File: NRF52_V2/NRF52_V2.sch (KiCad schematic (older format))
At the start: 0 parts

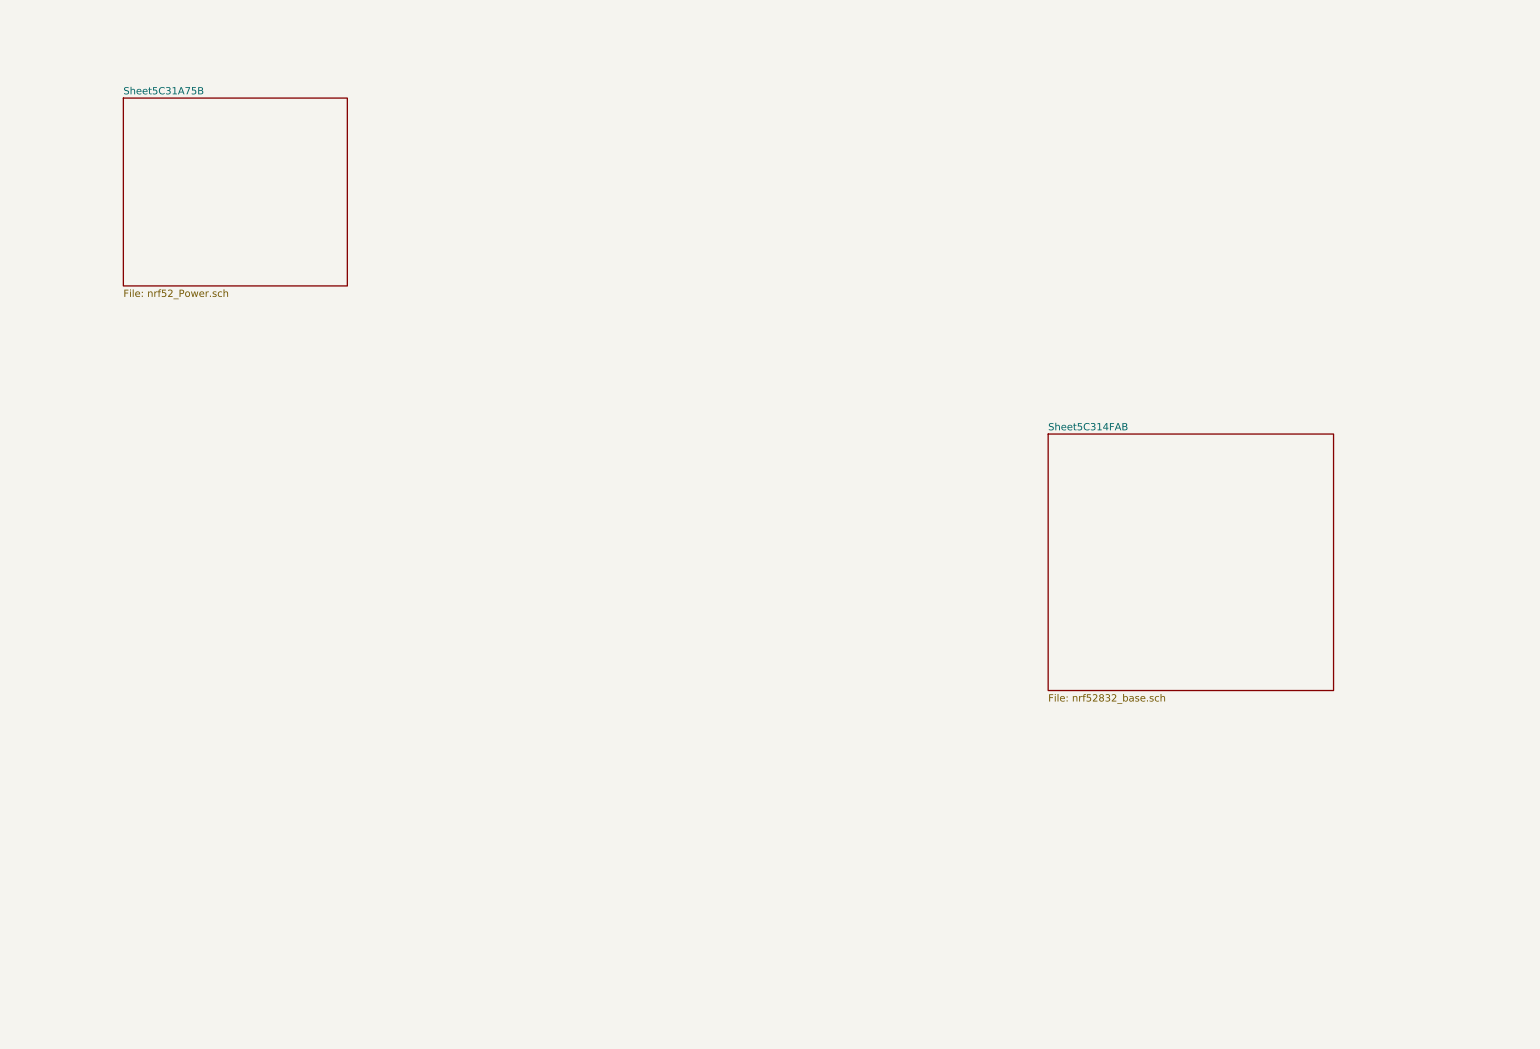
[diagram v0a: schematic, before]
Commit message: Added SWD header and some buttons
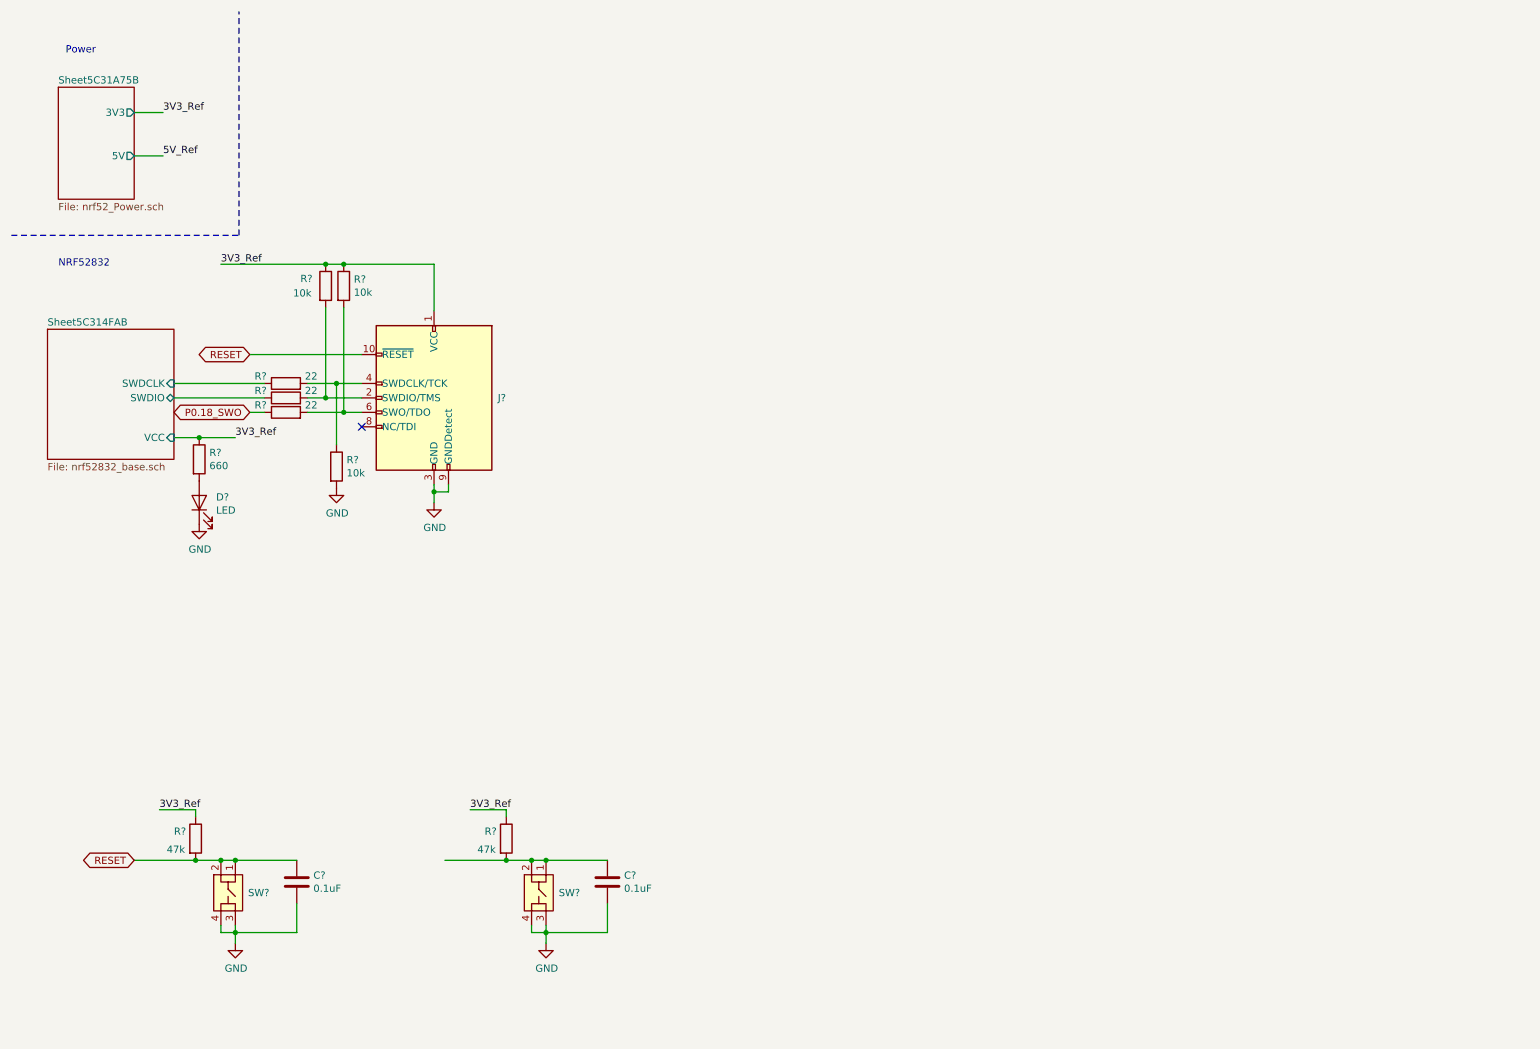
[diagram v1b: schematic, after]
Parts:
- added C? (x2): 0.1uF, symbol Device:C
- added D?: LED, symbol Device:LED
- added J?: Conn_ARM_JTAG_SWD_10, Connector_PinHeader_1.27mm:PinHeader_2x05_P1.27mm_Vertical_SMD, symbol Connector:Conn_ARM_JTAG_SWD_10
- added R? (x2): 47k, symbol Device:R
- added R?: 660, symbol Device:R
- added R? (x3): 22, symbol Device:R
- added R? (x3): 10k, symbol Device:R
- added SW? (x2): SW_SPST_4pin, symbol Project_Libary:SW_SPST_4pin
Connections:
- new net: C?.1, R?.2, SW?.1, SW?.2
- new net: D?.2 (A), R?.2
- new net: J?.2 (SWDIO/TMS), R?.2, R?.2
- new net: J?.4 (SWDCLK/TCK), R?.1, R?.2
- new net: J?.6 (SWO/TDO), R?.2, R?.2
- new net 3V3_Ref: J?.1 (VCC), R?.1, R?.1, R?.1, R?.1, R?.1
- new net GND: C?.2, C?.2, D?.1 (K), J?.3 (GND), J?.5 (GND), J?.9 (GNDDetect), R?.2, SW?.3, SW?.3, SW?.4, SW?.4
- new net P0.18_SWO: R?.1
- new net RESET: C?.1, J?.10 (~RESET~), R?.2, SW?.1, SW?.2
- new net Sheet5C314FAB/SWDCLK: R?.1
- new net Sheet5C314FAB/SWDIO: R?.1
- no-connect marks 0 -> 1
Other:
- note added: "NRF52832"
- note added: "Power"

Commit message: Added GPIO pin headers, buttons, and LEDs.
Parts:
- added D? (x2): LED, symbol Device:LED
- added J?: Conn_01x04_Male, symbol Connector:Conn_01x04_Male
- added J? (x2): Conn_01x05_Male, symbol Connector:Conn_01x05_Male
- added J? (x2): Conn_01x10_Male, symbol Connector:Conn_01x10_Male
- added R? (x2): 660, symbol Device:R
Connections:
- net 3V3_Ref: now also J?.9 (Pin_9); no longer J?.1 (VCC), R?.1, R?.1
- net 5V_Ref: now also J?.1 (VCC), R?.1, R?.1, J?.10 (Pin_10)
- net GND: now also D?.1 (K), D?.1 (K), J?.4 (Pin_4), J?.5 (Pin_5)
- net P0.18_SWO: now also J?.8 (Pin_8)
- net P0.24: now reaches C?.1, R?.2, SW?.1, SW?.2
- net P0.24: now also J?.3 (Pin_3)
- new net: D?.2 (A), R?.2 (x2)
- new net P0.02: J?.1 (Pin_1)
- new net P0.03: J?.2 (Pin_2)
- new net P0.04: J?.3 (Pin_3), R?.1
- new net P0.05: J?.4 (Pin_4), R?.1
- new net P0.06: J?.1 (Pin_1)
- new net P0.07: J?.2 (Pin_2)
- new net P0.08: J?.3 (Pin_3)
- new net P0.09: J?.4 (Pin_4)
- new net P0.10: J?.5 (Pin_5)
- new net P0.11_SDA: J?.1 (Pin_1)
- new net P0.12_SCL: J?.2 (Pin_2)
- new net P0.13: J?.3 (Pin_3)
- new net P0.14: J?.4 (Pin_4)
- new net P0.15: J?.5 (Pin_5)
- new net P0.16: J?.6 (Pin_6)
- new net P0.17: J?.7 (Pin_7)
- new net P0.19: J?.9 (Pin_9)
- new net P0.20: J?.10 (Pin_10)
- new net P0.22: J?.1 (Pin_1)
- new net P0.23: J?.2 (Pin_2)
- new net P0.25: J?.2 (Pin_2)
- new net P0.26: J?.3 (Pin_3)
- new net P0.27: J?.4 (Pin_4)
- new net P0.28: J?.5 (Pin_5)
- new net P0.29: J?.6 (Pin_6)
- new net P0.30: J?.7 (Pin_7)
- new net P0.31: J?.8 (Pin_8)
- new net V+: J?.1 (Pin_1)
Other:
- note added: "User I/O"
- moved on the sheet: C?, R?, SW?

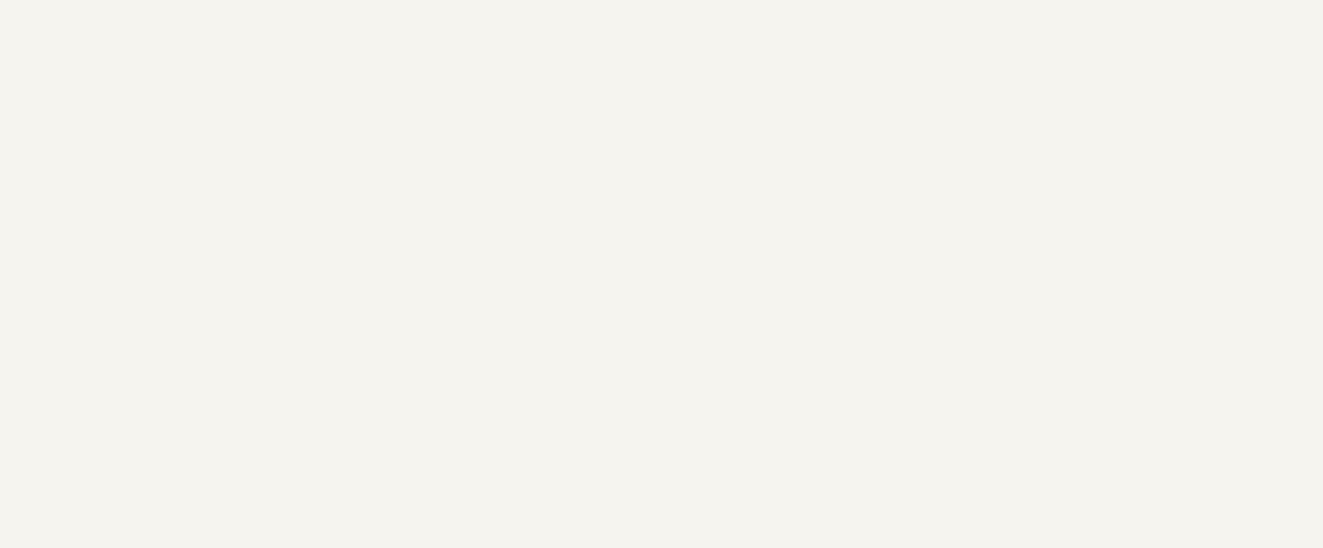
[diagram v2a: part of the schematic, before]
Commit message: Added EEPROM 4KB and photo sensor to schematic.
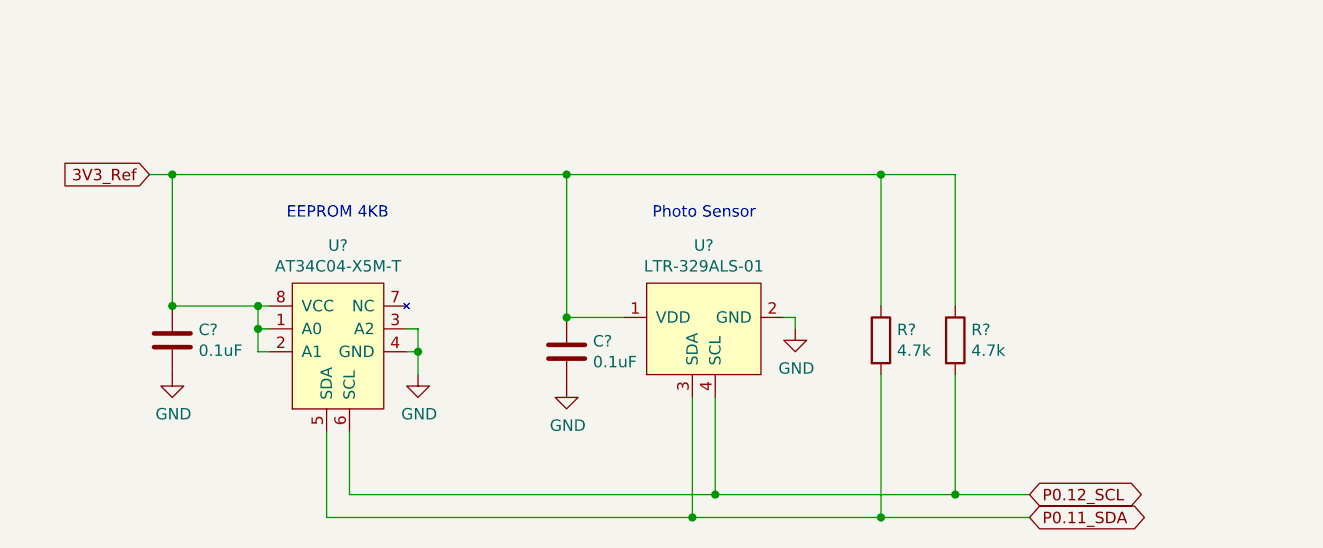
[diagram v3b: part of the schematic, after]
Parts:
- added C? (x2): 0.1uF, symbol Device:C
- added R? (x2): 4.7k, symbol Device:R
- added U?: AT34C04-X5M-T, symbol Project_Libary:AT34C04-X5M-T
- added U?: LTR-329ALS-01, symbol Project_Libary:LTR-329ALS-01
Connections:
- net 3V3_Ref: now also C?.1, C?.1, R?.1, R?.1, U?.1 (A0), U?.1 (VDD), U?.2 (A1), U?.8 (VCC)
- net GND: now also C?.2, C?.2, U?.2 (GND), U?.3 (A2), U?.4 (GND)
- net P0.11_SDA: now also R?.2, U?.3 (SDA), U?.5 (SDA)
- net P0.12_SCL: now also R?.2, U?.4 (SCL), U?.6 (SCL)
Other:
- note added: "EEPROM 4KB"
- note added: "Photo Sensor"
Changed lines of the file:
@@
 Text Notes 7800 1900 0    50   ~ 0
 User I/O
+$Comp
+L Project_Libary:AT34C04-X5M-T U?
+U 1 1 5C344423
+P 1875 6650
+F 0 "U?" H 1875 6965 50  0000 C CNN
+F 1 "AT34C04-X5M-T" H 1875 6874 50  0000 C CNN
+F 2 "" H 1825 7150 50  0001 C CNN
+F 3 "" H 1825 7150 50  0001 C CNN
+	1    1875 6650
+	1    0    0    -1
+$EndComp
+$Comp
+L Project_Libary:LTR-329ALS-01 U?
+U 1 1 5C344509
+P 3475 6700
+F 0 "U?" H 3475 7065 50  0000 C CNN
+F 1 "LTR-329ALS-01" H 3475 6974 50  0000 C CNN
+F 2 "" H 3475 6800 50  0001 C CNN
+F 3 "" H 3475 6800 50  0001 C CNN
+	1    3475 6700
+	1    0    0    -1
+$EndComp
+$Comp
+L Device:C C?
+U 1 1 5C3444A4
+P 1150 6750
+F 0 "C?" H 1265 6796 50  0000 L CNN
+F 1 "0.1uF" H 1265 6705 50  0000 L CNN
+F 2 "" H 1188 6600 50  0001 C CNN
+F 3 "~" H 1150 6750 50  0001 C CNN
+	1    1150 6750
+	1    0    0    -1
+$EndComp
+$Comp
+L Device:C C?
+U 1 1 5C34454E
+P 2875 6800
+F 0 "C?" H 2990 6846 50  0000 L CNN
+F 1 "0.1uF" H 2990 6755 50  0000 L CNN
+F 2 "" H 2913 6650 50  0001 C CNN
+F 3 "~" H 2875 6800 50  0001 C CNN
+	1    2875 6800
+	1    0    0    -1
+$EndComp
+Text Notes 1650 6225 0    50   ~ 0
+EEPROM 4KB
+Text Notes 3250 6225 0    50   ~ 0
+Photo Sensor
+Text GLabel 4900 7525 2    50   BiDi ~ 0
+P0.11_SDA
+Text GLabel 4900 7425 2    50   BiDi ~ 0
+P0.12_SCL
+Text GLabel 1050 6025 0    50   Input ~ 0
+3V3_Ref
+$Comp
+L Device:R R?
+U 1 1 5C344E76
+P 4250 6750
+F 0 "R?" H 4320 6796 50  0000 L CNN
+F 1 "4.7k" H 4320 6705 50  0000 L CNN
+F 2 "" V 4180 6750 50  0001 C CNN
+F 3 "~" H 4250 6750 50  0001 C CNN
+	1    4250 6750
+	1    0    0    -1
+$EndComp
+$Comp
+L Device:R R?
+U 1 1 5C344FD3
+P 4575 6750
+F 0 "R?" H 4645 6796 50  0000 L CNN
+F 1 "4.7k" H 4645 6705 50  0000 L CNN
+F 2 "" V 4505 6750 50  0001 C CNN
+F 3 "~" H 4575 6750 50  0001 C CNN
+	1    4575 6750
+	1    0    0    -1
+$EndComp
+Wire Wire Line
+	4575 6025 4575 6600
+Wire Wire Line
+	4250 6600 4250 6025
+Wire Wire Line
+	1050 6025 1150 6025
+Connection ~ 4250 6025
+Wire Wire Line
+	4250 6025 4575 6025
+Wire Wire Line
+	1150 6600 1150 6025
+Connection ~ 1150 6025
+Wire Wire Line
+	1150 6025 2875 6025
+Wire Wire Line
+	1575 6600 1525 6600
+Connection ~ 1150 6600
+Wire Wire Line
+	1575 6700 1525 6700
+Wire Wire Line
+	1525 6700 1525 6600
+Connection ~ 1525 6600
+Wire Wire Line
+	1525 6600 1150 6600
+Wire Wire Line
+	1575 6800 1525 6800
+Wire Wire Line
+	1525 6800 1525 6700
+Connection ~ 1525 6700
+Wire Wire Line
+	3125 6650 2875 6650
+Wire Wire Line
+	2875 6650 2875 6025
+Connection ~ 2875 6650
+Connection ~ 2875 6025
+Wire Wire Line
+	2875 6025 4250 6025
+Wire Wire Line
+	4900 7425 4575 7425
+Wire Wire Line
+	1925 7425 1925 7150
+Wire Wire Line
+	3525 7425 3525 7000
+Connection ~ 3525 7425
+Wire Wire Line
+	3525 7425 1925 7425
+Wire Wire Line
+	4900 7525 4250 7525
+Wire Wire Line
+	1825 7525 1825 7150
+Wire Wire Line
+	3425 7000 3425 7525
+Connection ~ 3425 7525
+Wire Wire Line
+	3425 7525 1825 7525
+Wire Wire Line
+	4250 6900 4250 7525
+Connection ~ 4250 7525
+Wire Wire Line
+	4250 7525 3425 7525
+Wire Wire Line
+	4575 6900 4575 7425
+Connection ~ 4575 7425
+Wire Wire Line
+	4575 7425 3525 7425
+$Comp
+L power:GND #PWR?
+U 1 1 5C357331
+P 1150 6900
+F 0 "#PWR?" H 1150 6650 50  0001 C CNN
+F 1 "GND" H 1155 6727 50  0000 C CNN
+F 2 "" H 1150 6900 50  0001 C CNN
+F 3 "" H 1150 6900 50  0001 C CNN
+	1    1150 6900
+	1    0    0    -1
+$EndComp
+$Comp
+L power:GND #PWR?
+U 1 1 5C3573B4
+P 2225 6900
+F 0 "#PWR?" H 2225 6650 50  0001 C CNN
+F 1 "GND" H 2230 6727 50  0000 C CNN
+F 2 "" H 2225 6900 50  0001 C CNN
+F 3 "" H 2225 6900 50  0001 C CNN
+	1    2225 6900
+	1    0    0    -1
+$EndComp
+$Comp
+L power:GND #PWR?
+U 1 1 5C3573FB
+P 2875 6950
+F 0 "#PWR?" H 2875 6700 50  0001 C CNN
+F 1 "GND" H 2880 6777 50  0000 C CNN
+F 2 "" H 2875 6950 50  0001 C CNN
+F 3 "" H 2875 6950 50  0001 C CNN
+	1    2875 6950
+	1    0    0    -1
+$EndComp
+$Comp
+L power:GND #PWR?
+U 1 1 5C3575E6
+P 3875 6700
+F 0 "#PWR?" H 3875 6450 50  0001 C CNN
+F 1 "GND" H 3880 6527 50  0000 C CNN
+F 2 "" H 3875 6700 50  0001 C CNN
+F 3 "" H 3875 6700 50  0001 C CNN
+	1    3875 6700
+	1    0    0    -1
+$EndComp
+Wire Wire Line
+	2225 6900 2225 6800
+Wire Wire Line
+	2225 6700 2175 6700
+Wire Wire Line
+	2175 6800 2225 6800
+Connection ~ 2225 6800
+Wire Wire Line
+	2225 6800 2225 6700
+Wire Wire Line
+	3875 6700 3875 6650
+Wire Wire Line
+	3875 6650 3825 6650
 $EndSCHEMATC
